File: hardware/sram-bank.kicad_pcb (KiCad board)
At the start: 2 copper layers, 50.8 x 78.7 mm, 48 parts, among them U1 74LVC138A, U10 74LVC8T245, U11 74LVC8T245, U12 IS66WV51216EALL, U13 74LVC138A, U2 74LVC8T245, U3 74LVC8T245, U4 74LVC8T245, U5 74LVC8T245, U6 74LVC8T245, U7 74LVC8T245, U8 74LVC8T245, U9 74LVC8T245

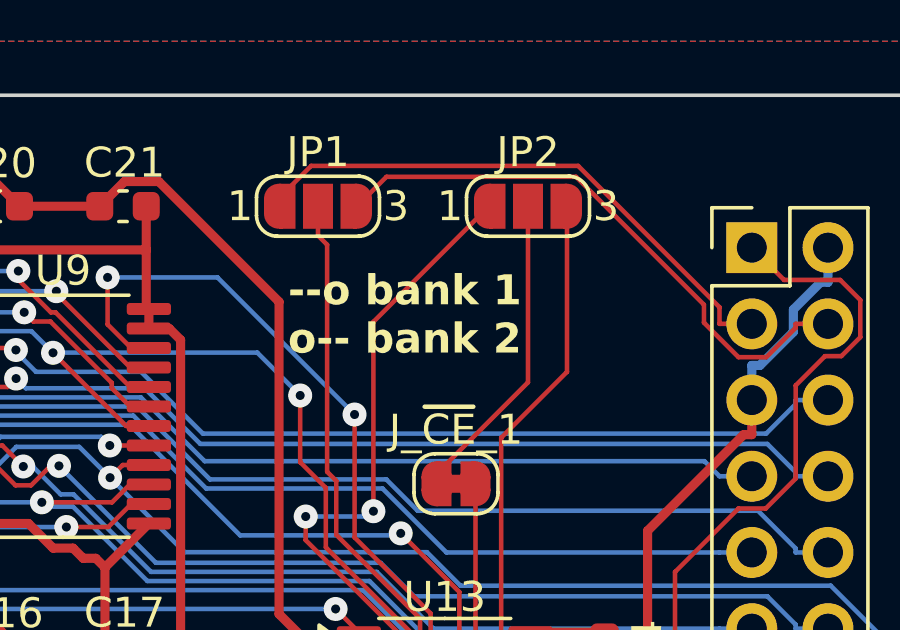
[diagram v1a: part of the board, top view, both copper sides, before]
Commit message: Be consistent with SRAM bank numbering (0-1, not 1-2)
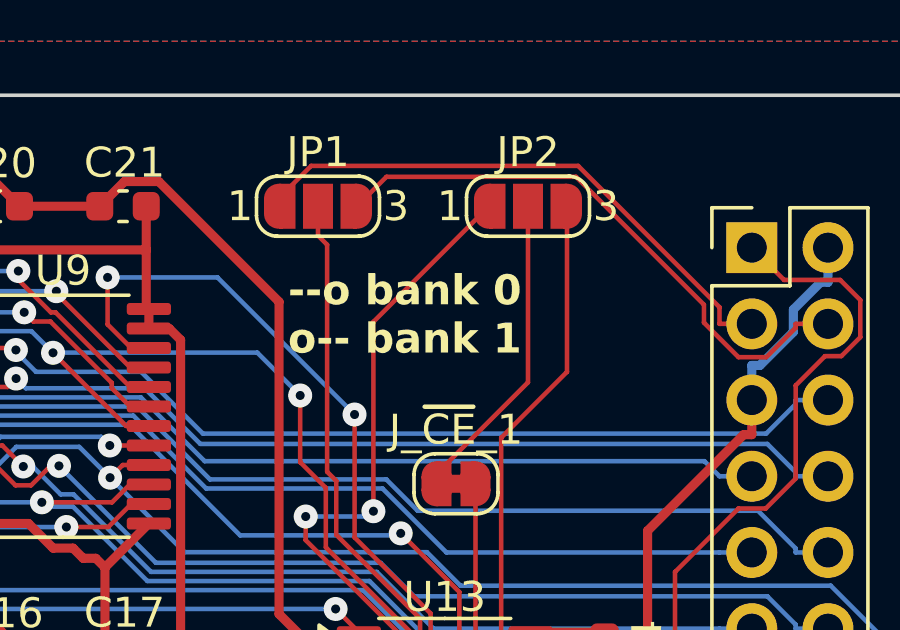
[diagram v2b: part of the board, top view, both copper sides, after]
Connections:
- J2 pad 3: /SRAM_DIS_1 -> /SRAM_DIS_0
- J2 pad 4: /SRAM_DIS_2 -> /SRAM_DIS_1
- JP1 pad 1: /SRAM_DIS_1 -> /SRAM_DIS_0
- JP1 pad 3: /SRAM_DIS_2 -> /SRAM_DIS_1
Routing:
- net /SRAM_DIS_2: track 19.5 -> 0.00 mm
- net /SRAM_DIS_0: track 0.00 -> 19.0 mm
- net /SRAM_DIS_1: track 19.0 -> 19.5 mm
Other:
- board text added: "--o bank 0 o-- bank 1"
- board text removed: "--o bank 1 o-- bank 2"
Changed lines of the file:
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@@
 	(net 55 "/SEGA_D6")
 	(net 56 "/SEGA_D1")
-	(net 57 "/SRAM_DIS_2")
+	(net 57 "/SRAM_DIS_1")
 	(net 58 "/SRAM_W_A11")
 	(net 59 "/SRAM_W_A3")
@@
 	(net 62 "/SRAM_D_IN12")
 	(net 63 "/SEGA_A12")
-	(net 64 "/SRAM_DIS_1")
+	(net 64 "/SRAM_DIS_0")
 	(net 65 "/SRAM_D_IN14")
 	(net 66 "/SEGA_A17")
@@
 			(size 1 0.5)
 			(layers "F.Cu" "F.Mask")
-			(net 64 "/SRAM_DIS_1")
+			(net 64 "/SRAM_DIS_0")
 			(pinfunction "A")
 			(pintype "passive")
@@
 			(size 1 0.5)
 			(layers "F.Cu" "F.Mask")
-			(net 57 "/SRAM_DIS_2")
+			(net 57 "/SRAM_DIS_1")
 			(pinfunction "B")
 			(pintype "passive")
@@
 			(layers "*.Cu" "*.Mask")
 			(remove_unused_layers no)
-			(net 64 "/SRAM_DIS_1")
-			(pinfunction "SRAM_DIS_1")
+			(net 64 "/SRAM_DIS_0")
+			(pinfunction "SRAM_DIS_0")
 			(pintype "passive")
 		)
@@
 			(layers "*.Cu" "*.Mask")
 			(remove_unused_layers no)
-			(net 57 "/SRAM_DIS_2")
-			(pinfunction "SRAM_DIS_2")
+			(net 57 "/SRAM_DIS_1")
+			(pinfunction "SRAM_DIS_1")
 			(pintype "passive")
 		)
@@
 		)
 	)
-	(gr_text "--o bank 1\no-- bank 2"
+	(gr_text "--o bank 0\no-- bank 1"
 		(at 49 28 0)
 		(layer "F.SilkS")

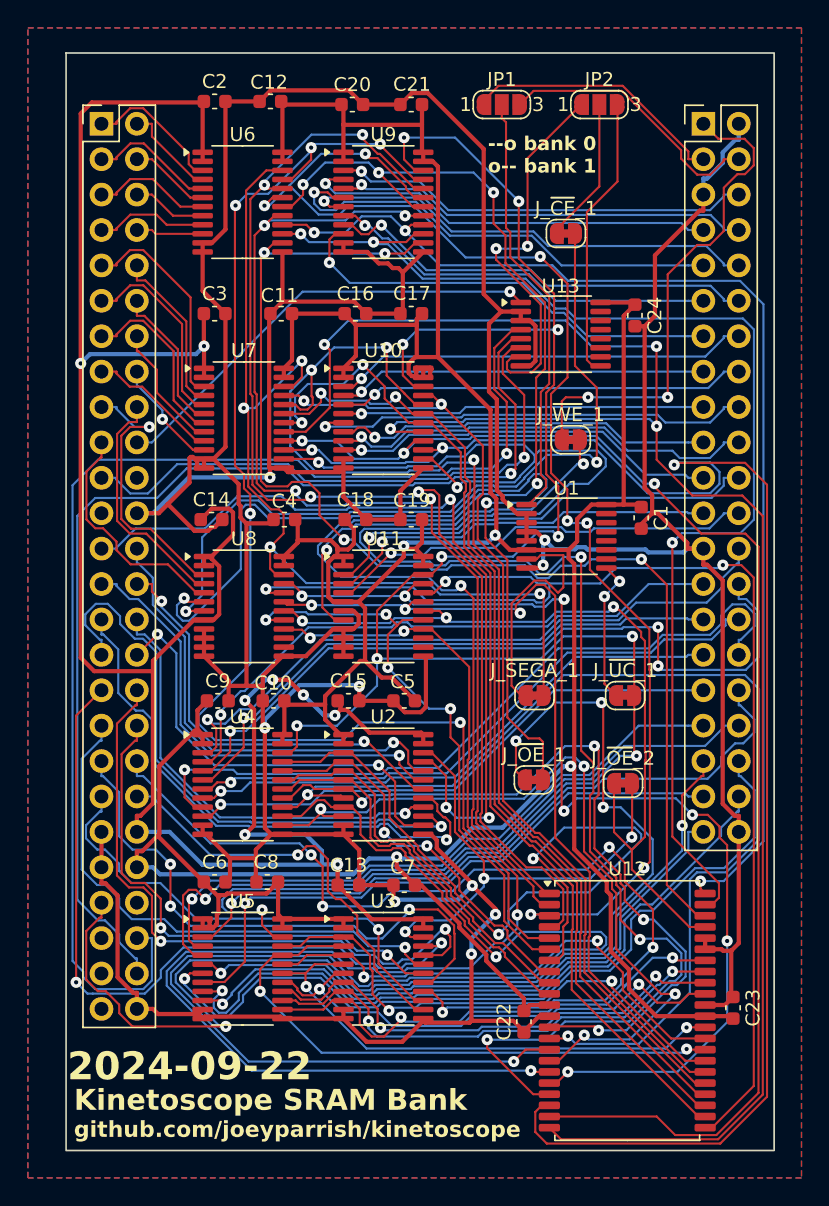
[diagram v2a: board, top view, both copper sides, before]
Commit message: Reroute SRAM board to match previous schematic changes
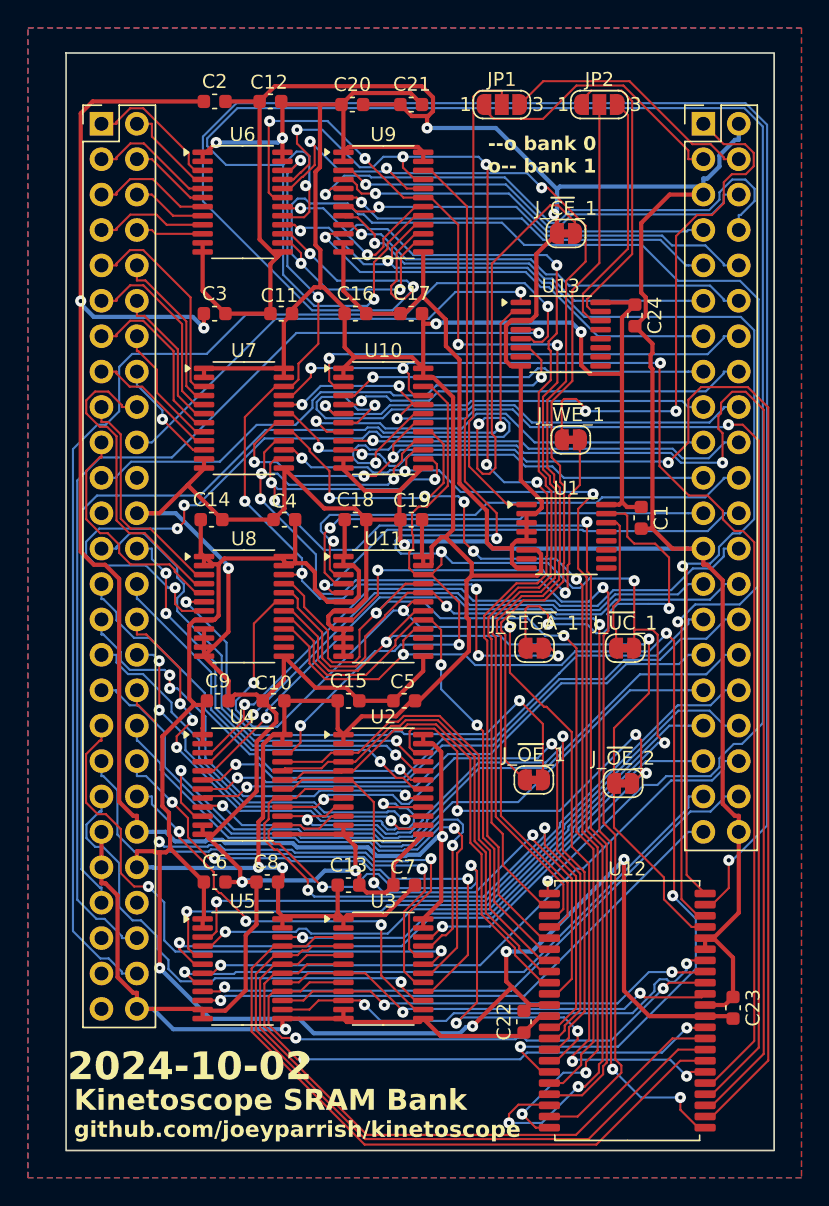
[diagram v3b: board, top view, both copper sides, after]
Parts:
- moved J_~{SEGA}_1 3.40 mm to (52.4, 62.0)
- moved J_~{UC}_1 3.40 mm to (58.9, 62.0)
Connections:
- C13 pad 1: +5V -> +3.3V
- C14 pad 1: +5V -> +3.3V
- C15 pad 1: +5V -> +3.3V
- JP2 pad 1: /~{SRAM_CE1} -> /~{SRAM_OE0}
- JP2 pad 2: /~{SRAM_CE} -> /~{SRAM_OE}
- JP2 pad 3: /~{SRAM_CE2} -> /~{SRAM_OE1}
- J_~{CE}_1 pad 1: /~{SRAM_CE} -> GND
- J_~{OE}_1 pad 1: /~{SEGA_OE} -> /~{SRAM_OE}
- J_~{OE}_1 pad 2: /~{SEGA_OE_INT} -> /~{SRAM_OE_INT}
- J_~{OE}_2 pad 2: /~{SRAM_OE_INT} -> /~{SRAM_BUFFER_OE_INT}
- U1 pad 14: unconnected-(U1-~{Y1}-Pad14) -> /~{UC_CONTROL}
- U1 pad 15: unconnected-(U1-~{Y0}-Pad15) -> /~{SEGA_CONTROL}
- U1 pad 7: /~{SEGA_CONTROL} -> unconnected-(U1-~{Y7}-Pad7)
- U1 pad 9: /~{UC_CONTROL} -> unconnected-(U1-~{Y6}-Pad9)
- U13 pad 14: unconnected-(U13-~{Y1}-Pad14) -> /~{SRAM_OE1}
- U13 pad 15: unconnected-(U13-~{Y0}-Pad15) -> /~{SRAM_OE0}
- U13 pad 2: GND -> /~{SEGA_OE}
- U13 pad 7: /~{SRAM_CE1} -> unconnected-(U13-~{Y7}-Pad7)
- U13 pad 9: /~{SRAM_CE2} -> unconnected-(U13-~{Y6}-Pad9)
- U2 pad 22: /~{SRAM_OE_INT} -> /~{SRAM_BUFFER_OE_INT}
- U3 pad 22: /~{SRAM_OE_INT} -> /~{SRAM_BUFFER_OE_INT}
- U6 pad 1: +5V -> +3.3V
- U6 pad 2: +5V -> +3.3V
- U7 pad 1: +5V -> +3.3V
- U7 pad 2: +5V -> +3.3V
- U8 pad 1: +5V -> +3.3V
- U8 pad 2: +5V -> +3.3V
- U8 pad 6: /~{SEGA_OE_INT} -> /~{SRAM_OE_INT}
- U8 pad 8: +5V -> +3.3V
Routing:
- net /SRAM_A4: track 77.9 -> 144.1 mm, vias 4 -> 3
- net /~{SEGA_OE_INT}: track 65.0 -> 0.00 mm, vias 2 -> 0
- net /SRAM_A6: track 88.7 -> 142.9 mm
- net /~{SRAM_OE}: track 0.00 -> 53.7 mm
- net /SRAM_A12: track 132.0 -> 79.3 mm, vias 4 -> 7
- net /~{SRAM_BUFFER_OE_INT}: track 0.00 -> 51.0 mm, vias 0 -> 4
- net +5V: track 161.7 -> 112.6 mm, vias 8 -> 3
- net +3.3V: track 301.5 -> 349.5 mm, vias 4 -> 10
- net /SRAM_DATA6: track 95.7 -> 51.5 mm
- net /SRAM_A15: track 130.0 -> 87.9 mm, vias 5 -> 4
- net /SEGA_D13: track 70.4 -> 38.4 mm, vias 5 -> 3
- net /SRAM_DATA5: track 78.2 -> 46.4 mm
- net /SRAM_A14: track 112.4 -> 80.7 mm, vias 3 -> 5
- net /SRAM_A10: track 71.0 -> 101.8 mm, vias 2 -> 3
- net /SRAM_A11: track 74.8 -> 103.9 mm, vias 2 -> 4
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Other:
- board text added: "2024-10-02"
- board text removed: "2024-09-22"

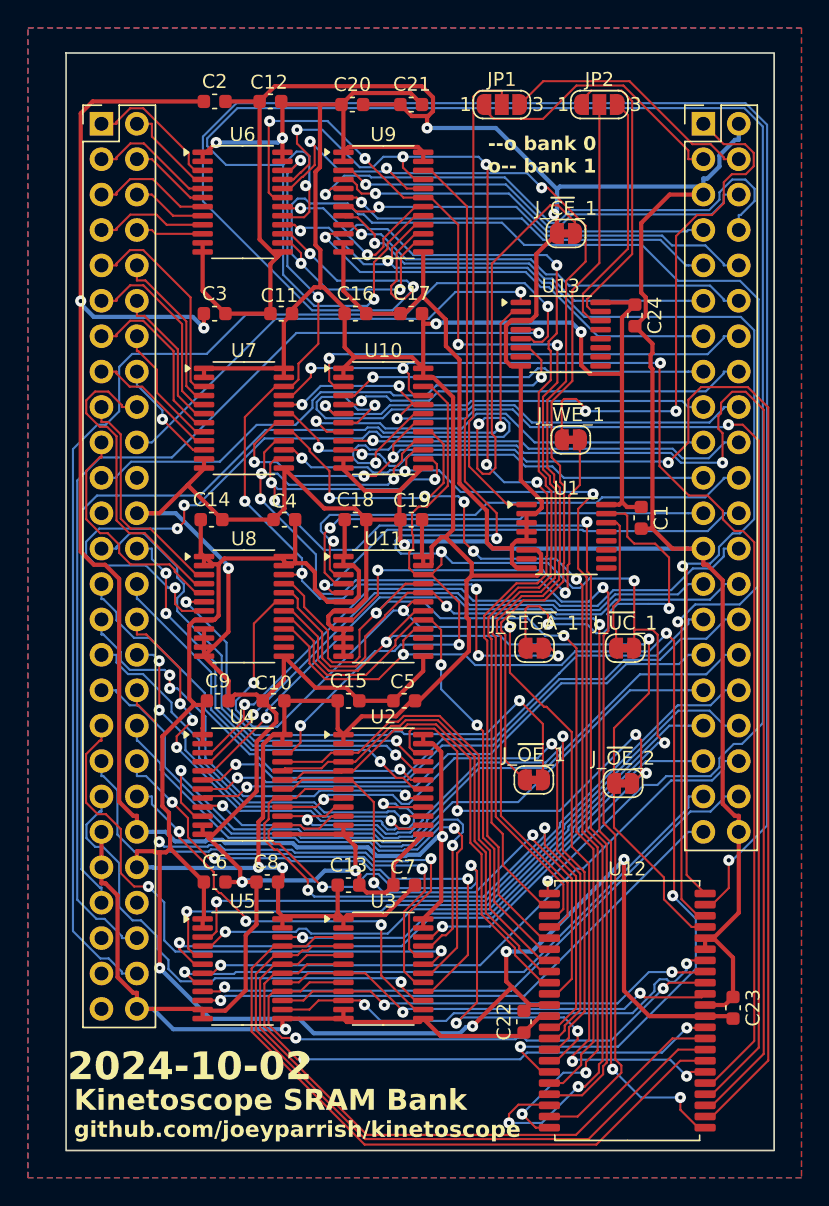
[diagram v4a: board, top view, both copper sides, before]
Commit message: Fix SRAM CE signaling
It turns out that a PSRAM's ~{CE} signal may not stay on at all times.
There is a maximum pulse width of 15us for this chipset, so that the
DRAM internal to the PSRAM can go through a refresh cycle.

Tying ~{CE} to ~{WE} (for writes) or ~{SEGA_CE} (for reads) seems to
meet all the timing requirements.  This has yet to be verified,
though, for a lack of test pads for all ~{CE} signals on the previous
board revision.

(PCB routing in progress, will commit later.)
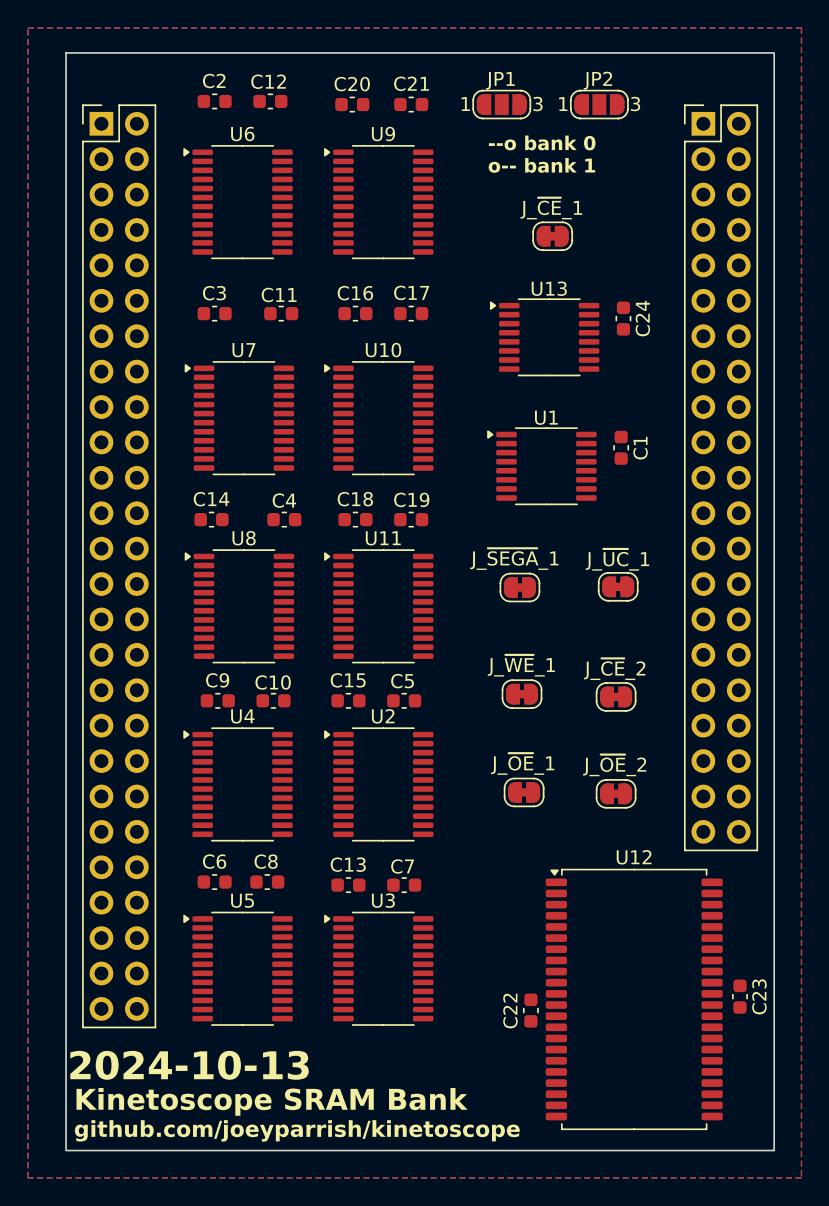
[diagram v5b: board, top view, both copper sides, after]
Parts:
- added J_~{CE}_2: ~, Jumper:SolderJumper-2_P1.3mm_Bridged_RoundedPad1.0x1.5mm, F.Cu at (58.2, 65.5)
- U12: value IS66WV51216EALL -> IS66WV51216EBLL
- moved J_~{WE}_1 18.6 mm to (51.5, 65.3)
- moved C1 5.23 mm to (58.6, 47.6)
- moved U1 5.23 mm to (53.2, 49.0)
- moved J_~{SEGA}_1 4.47 mm to (51.3, 57.6)
- moved J_~{UC}_1 4.43 mm to (58.4, 57.6)
- moved J_~{OE}_1 1.14 mm to (51.6, 72.3)
- moved J_~{CE}_1 0.97 mm to (53.6, 32.5)
- moved C22 0.94 mm to (52.1, 88.0)
- moved C23 0.94 mm to (67.1, 87.0)
- moved U12 0.94 mm to (59.5, 87.2)
- moved J_~{OE}_2 0.90 mm to (58.2, 72.5)
- moved U13 0.86 mm to (53.4, 39.7)
- moved C24 0.86 mm to (58.7, 38.4)
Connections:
- net /~{SRAM_CE_INT} renamed /~{SRAM_CE_READ_INT}
- J_~{CE}_1 pad 1: GND -> /~{SEGA_CE}
- U11 pad 7: GND -> /~{SRAM_CE_WRITE_INT}
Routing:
- net GND: track 441.9 -> 0.00 mm, vias 7 -> 0
- net +3.3V: track 349.5 -> 0.00 mm, vias 10 -> 0
- net /~{UC_CONTROL_INT}: track 145.7 -> 0.00 mm, vias 7 -> 0
- net /SRAM_A4: track 144.1 -> 0.00 mm, vias 3 -> 0
- net /SRAM_A6: track 142.9 -> 0.00 mm, vias 3 -> 0
- net +5V: track 112.6 -> 0.00 mm, vias 3 -> 0
- net /SRAM_A7: track 105.4 -> 0.00 mm, vias 3 -> 0
- net /SRAM_A11: track 103.9 -> 0.00 mm, vias 4 -> 0
- net /SRAM_A10: track 101.8 -> 0.00 mm, vias 3 -> 0
- net /SRAM_A13: track 91.5 -> 0.00 mm, vias 4 -> 0
- net /SRAM_A9: track 88.9 -> 0.00 mm, vias 4 -> 0
- net /SRAM_A8: track 88.7 -> 0.00 mm, vias 3 -> 0
- net /SRAM_A1: track 88.0 -> 0.00 mm, vias 3 -> 0
- net /SRAM_A15: track 87.9 -> 0.00 mm, vias 4 -> 0
- net /SRAM_A0: track 86.8 -> 0.00 mm, vias 5 -> 0
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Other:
- board text added: "2024-10-13"
- board text removed: "2024-10-02"

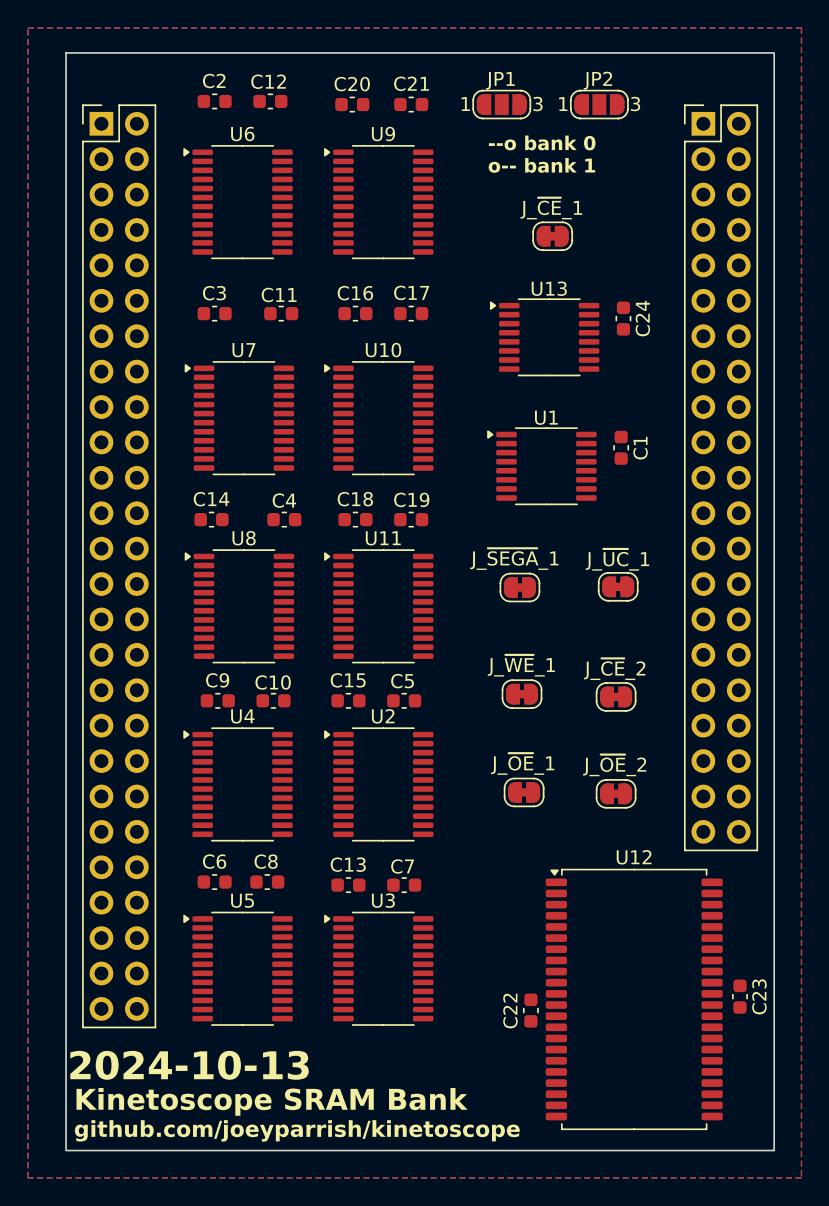
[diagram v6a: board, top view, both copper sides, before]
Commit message: Routing for SRAM bank PCB changes
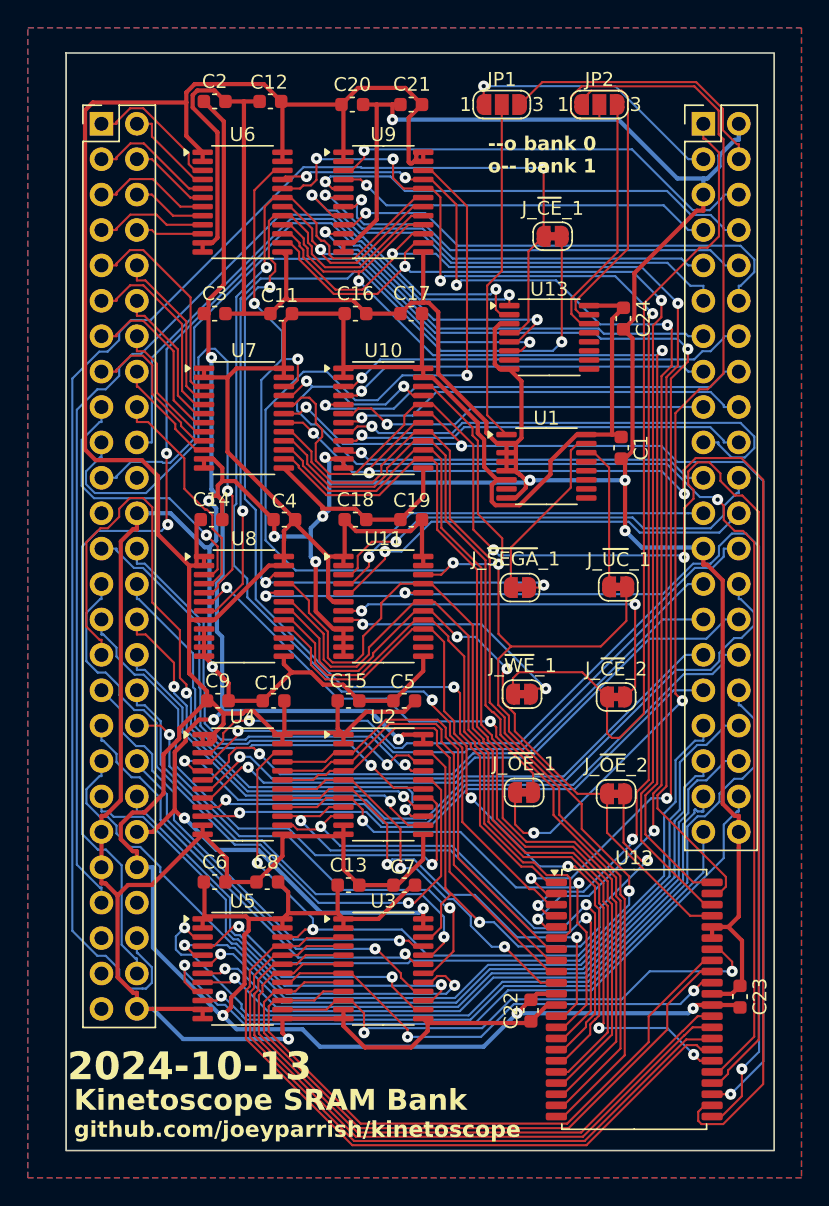
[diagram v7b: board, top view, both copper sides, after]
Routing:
- net GND: track 0.00 -> 435.5 mm, vias 0 -> 11
- net +3.3V: track 0.00 -> 345.7 mm, vias 0 -> 3
- net /~{UC_CONTROL_INT}: track 0.00 -> 162.2 mm, vias 0 -> 6
- net /~{SEGA_CE}: track 0.00 -> 104.9 mm, vias 0 -> 1
- net /SRAM_A9: track 0.00 -> 100.8 mm, vias 0 -> 2
- net +5V: track 0.00 -> 96.8 mm, vias 0 -> 5
- net /SRAM_A11: track 0.00 -> 96.1 mm, vias 0 -> 3
- net /SRAM_A8: track 0.00 -> 90.9 mm, vias 0 -> 3
- net /SRAM_A3: track 0.00 -> 90.6 mm, vias 0 -> 4
- net /~{SEGA_AS}: track 0.00 -> 88.1 mm, vias 0 -> 3
- net /SRAM_A10: track 0.00 -> 86.9 mm, vias 0 -> 3
- net /SRAM_A1: track 0.00 -> 86.4 mm, vias 0 -> 6
- net /SRAM_A0: track 0.00 -> 85.6 mm, vias 0 -> 6
- net /SRAM_A17: track 0.00 -> 83.5 mm, vias 0 -> 3
- net /SRAM_A6: track 0.00 -> 81.8 mm, vias 0 -> 2
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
